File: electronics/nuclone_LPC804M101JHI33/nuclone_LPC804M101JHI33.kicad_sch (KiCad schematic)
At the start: 41 parts

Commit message: switched from testpins to debug connector
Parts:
- removed TP1, TP2, TP3, TP4, TP5: (no value), symbol SquantorProto:testpad
- C1, C2: value (none) -> 10u; footprint (none) -> SquantorRcl:C_0603
- C14: value (none) -> 10n; footprint (none) -> SquantorRcl:C_0402
- C17: value (none) -> 1u; footprint (none) -> SquantorRcl:C_0603
- C4: value (none) -> 1u; footprint (none) -> SquantorRcl:C_0402
- C9: value (none) -> 100n; footprint (none) -> SquantorRcl:C_0805
- D2: value (none) -> GREEN; footprint (none) -> SquantorDiodes:LED_0603_hand
- F1: value (none) -> 0.5A; footprint (none) -> SquantorRcl:F_0603_hand
- FB1: value (none) -> 600; footprint (none) -> SquantorRcl:L_0603
- H1, H2, H3, H4: value (none) -> MountingHole; footprint (none) -> MountingHole:MountingHole_3.2mm_M3_Pad_Via
- J1: value (none) -> JTAG_2X05; footprint (none) -> SquantorConnectors:Header-0127-2X05-H006
- J2: value (none) -> TYPE-C-31-M-12; footprint (none) -> SquantorUsb:USB-C-HRO-31-M-12
- J3: value (none) -> nuclone_small_left; footprint (none) -> SquantorConnectorsNamed:nuclone_small_left_stacked
- J4: value (none) -> nuclone_small_right; footprint (none) -> SquantorConnectorsNamed:nuclone_small_right_stacked
- N1: value (none) -> OHWLOGO; footprint (none) -> Symbols:OSHW-Symbol_6.7x6mm_SilkScreen
- N2: value (none) -> V20220214; footprint (none) -> SquantorLabels:Label_Generic
- N3: value (none) -> JLCJLCJLCJLC; footprint (none) -> SquantorLabels:Label_Generic
- N4: value (none) -> NuClone LPC804M101JHI33; footprint (none) -> SquantorLabels:Label_Generic
- N5: value (none) -> Nuclone Template 20220213; footprint (none) -> SquantorLabels:Label_Generic
- R1, R7: value (none) -> 5.1K; footprint (none) -> SquantorRcl:R_0402_hand
- R13: value (none) -> 100; footprint (none) -> SquantorRcl:R_0402_hand
- R14: value (none) -> 1K; footprint (none) -> SquantorRcl:R_0402_hand
- R2, R3, R4, R5, R6: value (none) -> 47K; footprint (none) -> SquantorRcl:R_0402_hand
- R8: value (none) -> 10K; footprint (none) -> SquantorRcl:R_0402_hand
- SW1: value (none) -> RESET; footprint (none) -> SquantorSwitches:TD-85XU
- SW2: value (none) -> Bootloader; footprint (none) -> SquantorSwitches:TD-85XU
- U1: value (none) -> MCP1702-MB; footprint (none) -> SquantorIC:SOT89-NXP
- U2: value (none) -> TPESD0504C6; footprint (none) -> SquantorIC:SOT363-ONsemi
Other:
- moved on the sheet: C14, R13, SW1

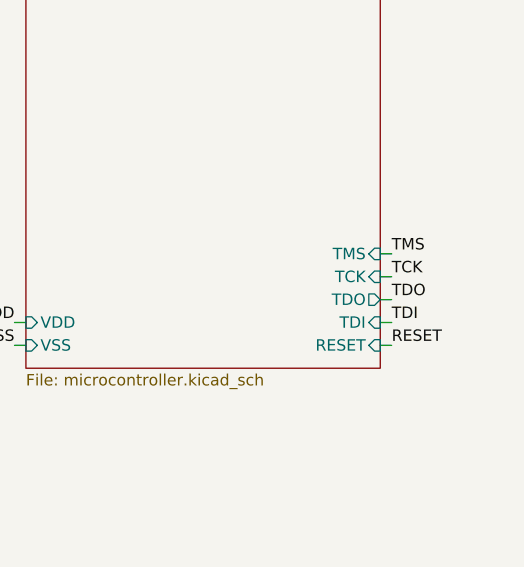
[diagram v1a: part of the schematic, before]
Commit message: changed test points to a connector for logic analyser
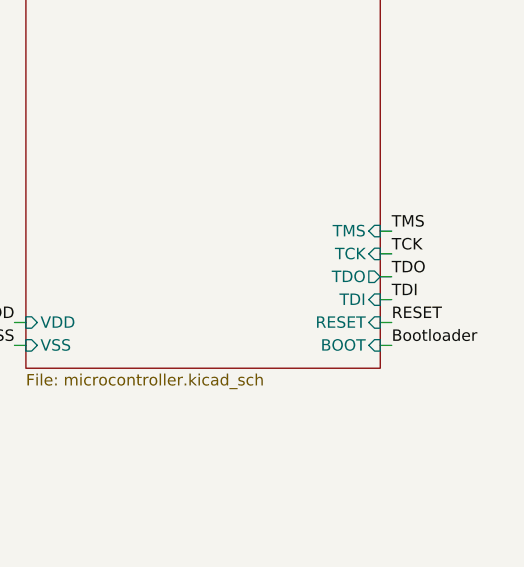
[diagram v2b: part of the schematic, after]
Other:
- sheet microcontroller ports: added BOOT; removed none

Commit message: reviewed
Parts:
- N2: value V20220214 -> V20220912
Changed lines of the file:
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@@
       (effects (font (size 1.524 1.524)) (justify left))
     )
-    (property "Value" "V20220214" (id 1) (at 17.78 182.88 0)
+    (property "Value" "V20220912" (id 1) (at 17.78 182.88 0)
       (effects (font (size 1.524 1.524)) (justify left))
     )
@@
     )
     (path "/00000000-0000-0000-0000-00005d6a68b9"
-      (reference "N2") (unit 1) (value "V20220214") (footprint "SquantorLabels:Label_Generic")
+      (reference "N2") (unit 1) (value "V20220912") (footprint "SquantorLabels:Label_Generic")
     )
     (path "/00000000-0000-0000-0000-00005d8b1b32"
